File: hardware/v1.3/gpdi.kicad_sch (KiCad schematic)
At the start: 20 parts, among them J2 HDMI_C_1.3, U1 ECP5-CABGA256, U5 PCA9306DC1

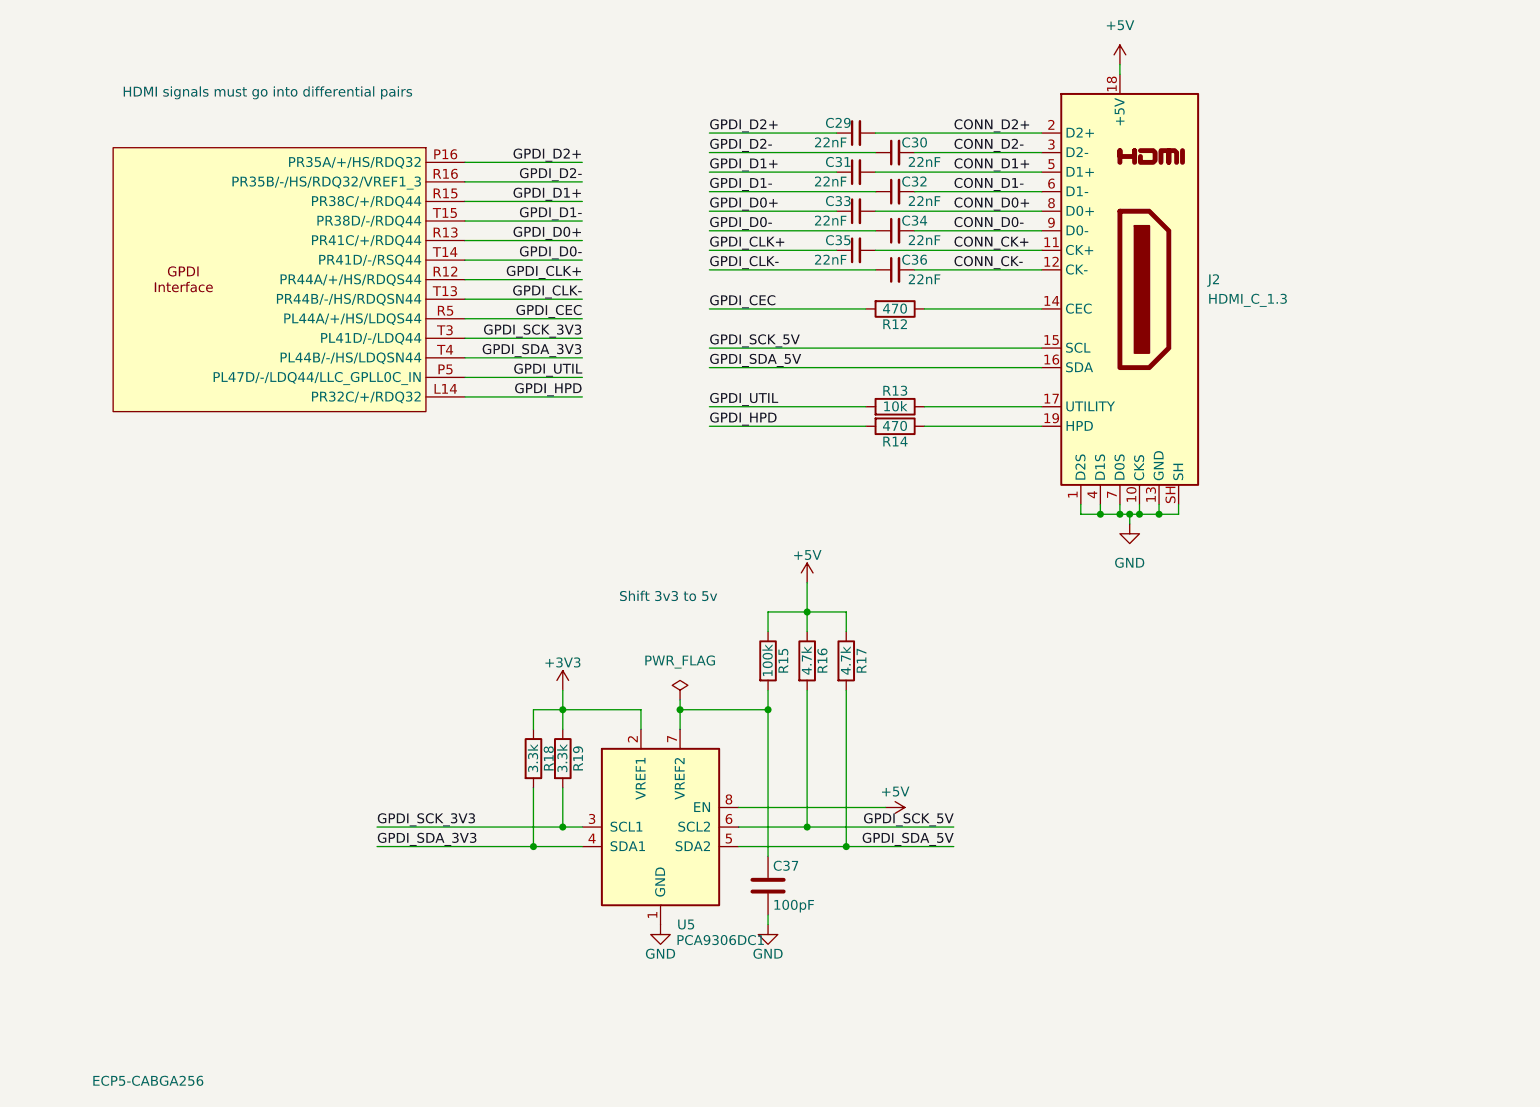
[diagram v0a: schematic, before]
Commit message: Refine README
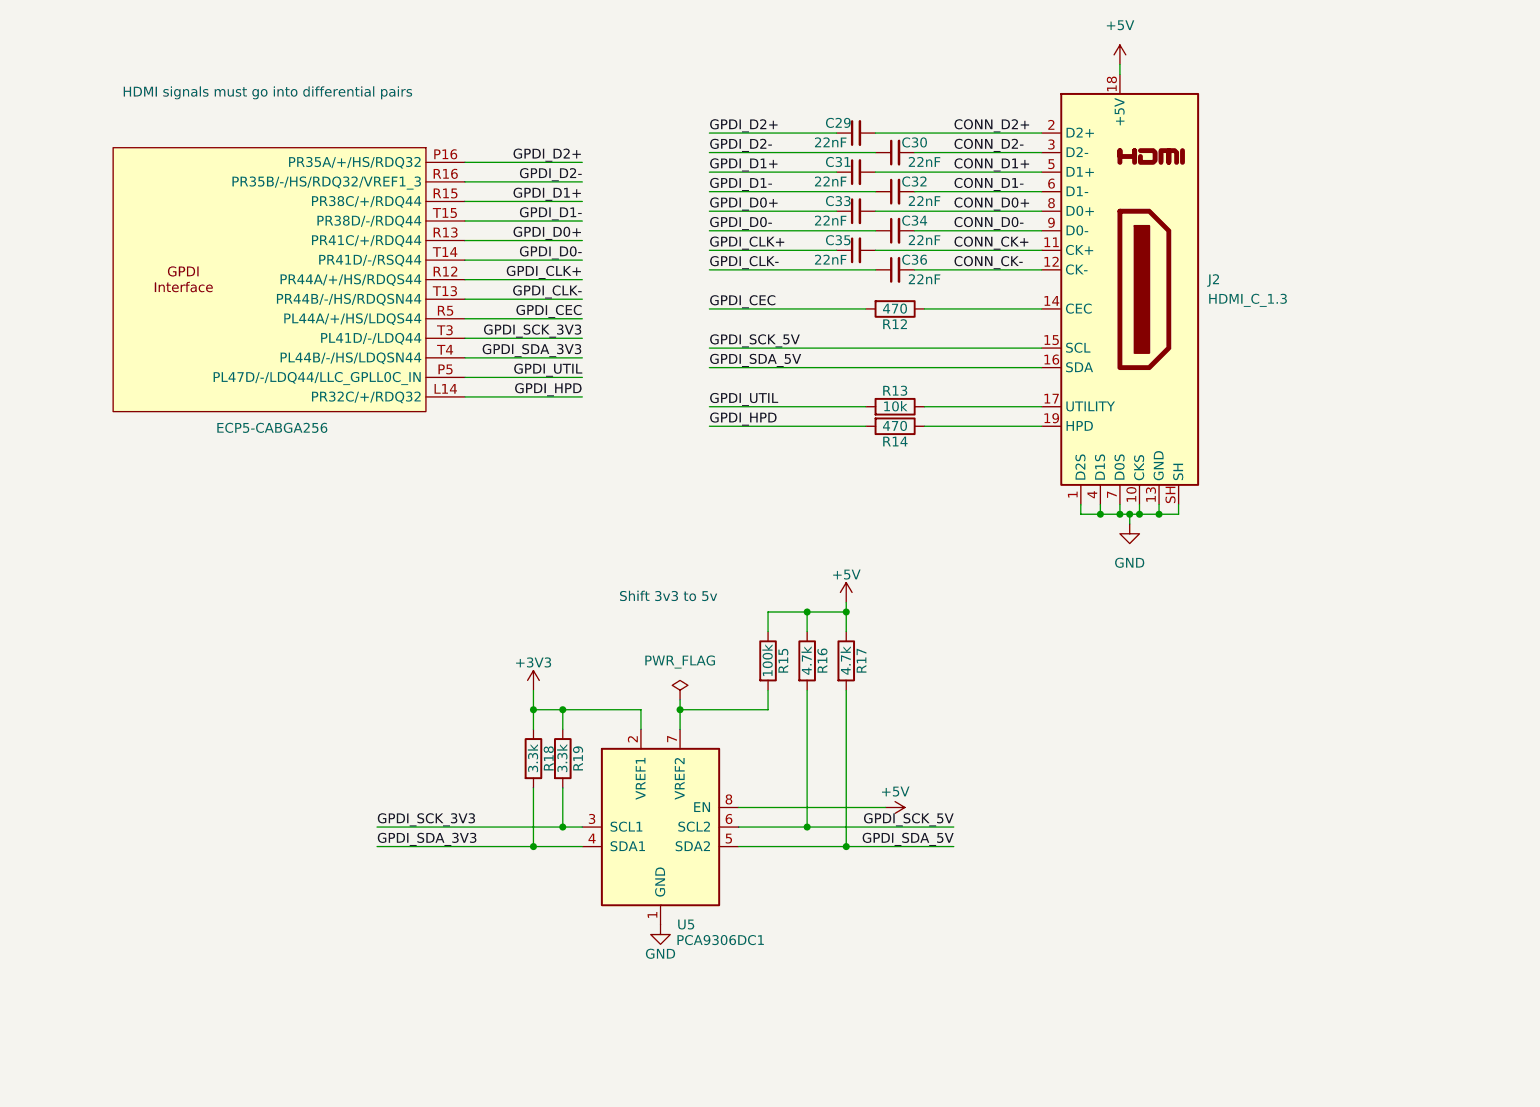
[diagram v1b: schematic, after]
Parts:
- removed C37: 100pF, Capacitor_SMD:C_0402_1005Metric, symbol Device:C
- C29, C30, C31, C32, C33, C34, C35, C36: LCSC Link (none) -> https://lcsc.com/product-detail/Multilayer-Ceramic-Capacito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; Manufactuer Part Number (none) -> 0402B223K500NT
- J2: LCSC Link (none) -> https://lcsc.com/product-detail/HDMI-Connectors_XKB-Connect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; Manufactuer Part Number (none) -> A71-05H4-111N1
- R12, R14: LCSC Link (none) -> https://lcsc.com/product-detail/Chip-Resistor-Surface-Mount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; Manufactuer Part Number (none) -> 0402WGF4700TCE
- R13: LCSC Link (none) -> https://lcsc.com/product-detail/Chip-Resistor-Surface-Mount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; Manufactuer Part Number (none) -> 0402WGF1002TCE
- R15: LCSC Link (none) -> https://lcsc.com/product-detail/Chip-Resistor-Surface-Mount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; Manufactuer Part Number (none) -> 0402WGF1003TCE
- R16, R17: LCSC Link (none) -> https://lcsc.com/product-detail/Chip-Resistor-Surface-Mount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; LCSC Part # C25900 -> C25900; Manufactuer Part Number (none) -> 0402WGF4701TCE
- R18, R19: LCSC Link (none) -> https://lcsc.com/product-detail/Chip-Resistor-Surface-Mount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; LCSC Part # C25890 -> C25890; Manufactuer Part Number (none) -> 0402WGF3301TCE
- U1: LCSC Link (none) -> https://lcsc.com/product-detail/Programmable-Logic-Device-C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; LCSC Part # (none) -> C1521614; Manufactuer Part Number (none) -> LFE5U-25F-6BG256C
- U5: LCSC Link (none) -> https://lcsc.com/product-detail/Translators-Level-Shifters_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; Manufactuer Part Number (none) -> PCA9306DC1

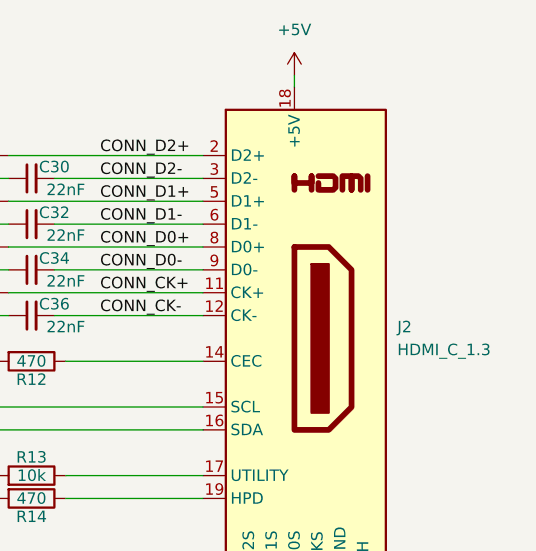
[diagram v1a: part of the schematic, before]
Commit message: Added start of documentation and changed GPDI
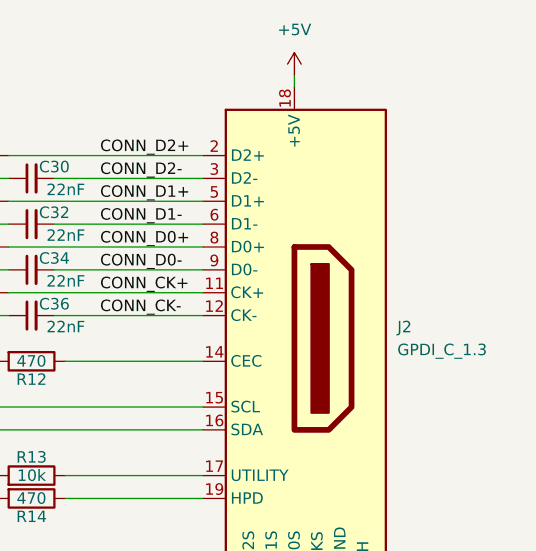
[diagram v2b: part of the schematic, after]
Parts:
- J2: value HDMI_C_1.3 -> GPDI_C_1.3; symbol Connector:HDMI_C_1.3 -> icepi-lib:GPDI_C_1.3
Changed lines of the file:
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@@
 	)
 	(symbol
-		(lib_id "Connector:HDMI_C_1.3")
+		(lib_id "icepi-lib:GPDI_C_1.3")
 		(at 196.85 77.47 0)
 		(unit 1)
@@
 			)
 		)
-		(property "Value" "HDMI_C_1.3"
+		(property "Value" "GPDI_C_1.3"
 			(at 208.28 78.7399 0)
 			(effects
@@
 			)
 		)
-		(property "Datasheet" "http://pinoutguide.com/PortableDevices/mini_hdmi_pinout.shtml"
+		(property "Datasheet" "-"
 			(at 197.485 77.47 0)
 			(effects
@@
 			)
 		)
-		(property "Description" "HDMI 1.3+ type C connector"
+		(property "Description" "GPDI type C connector"
 			(at 196.85 77.47 0)
 			(effects

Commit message: Update files
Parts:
- added U12: TPD2EUSB30A, Package_TO_SOT_SMD:Texas_DRT-3, symbol Power_Protection:TPD2EUSB30A
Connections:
- net GND: now also U12.3 (GND)
- net GPDI_HPD: now also U12.2 (D-)
- net GPDI_UTIL: now also U12.1 (D+)
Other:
- note added: "HDMI signals differential I/O pins"
- note added: "Signal filtering! UwU"
- note added: "Using USB TSV diode to BOM optimize Can be replaced with only one 3.6V zener on HPD line Protect I/O pins from 5V"
- note removed: "HDMI signals must go into differential pairs"
- moved on the sheet: C29, C30, C31, C32, C33, C34, C35, C36, J2, R12, R13, R14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

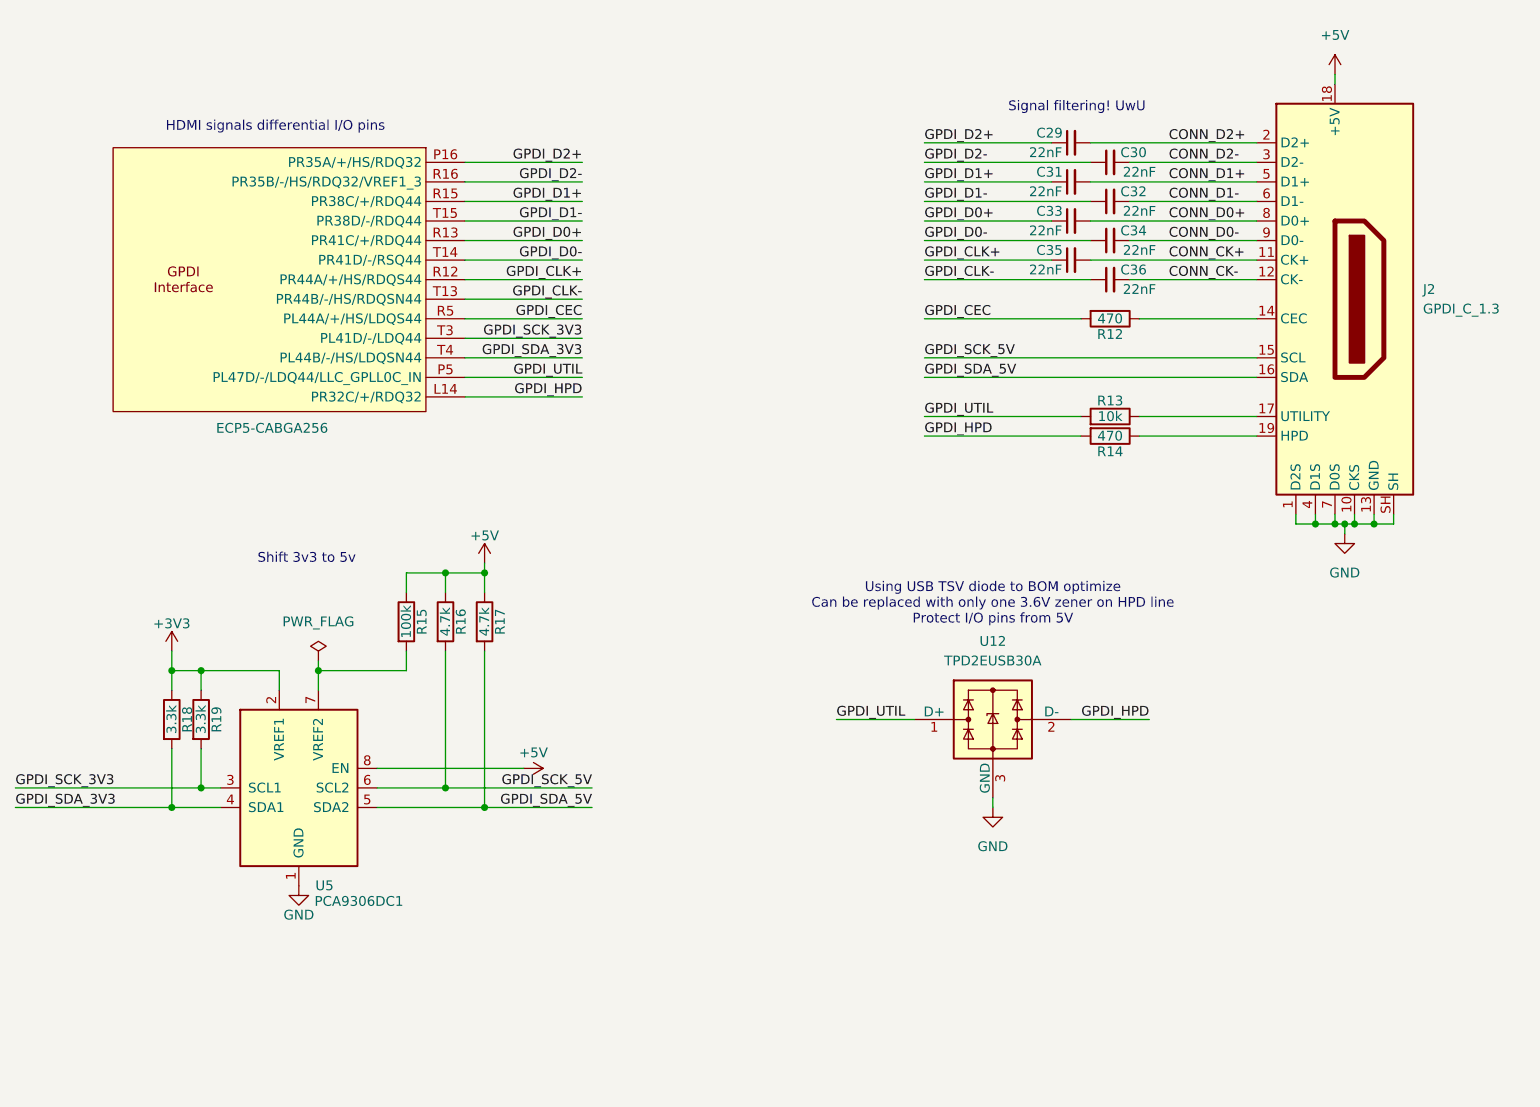
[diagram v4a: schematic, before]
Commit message: Improve makefile and hardware
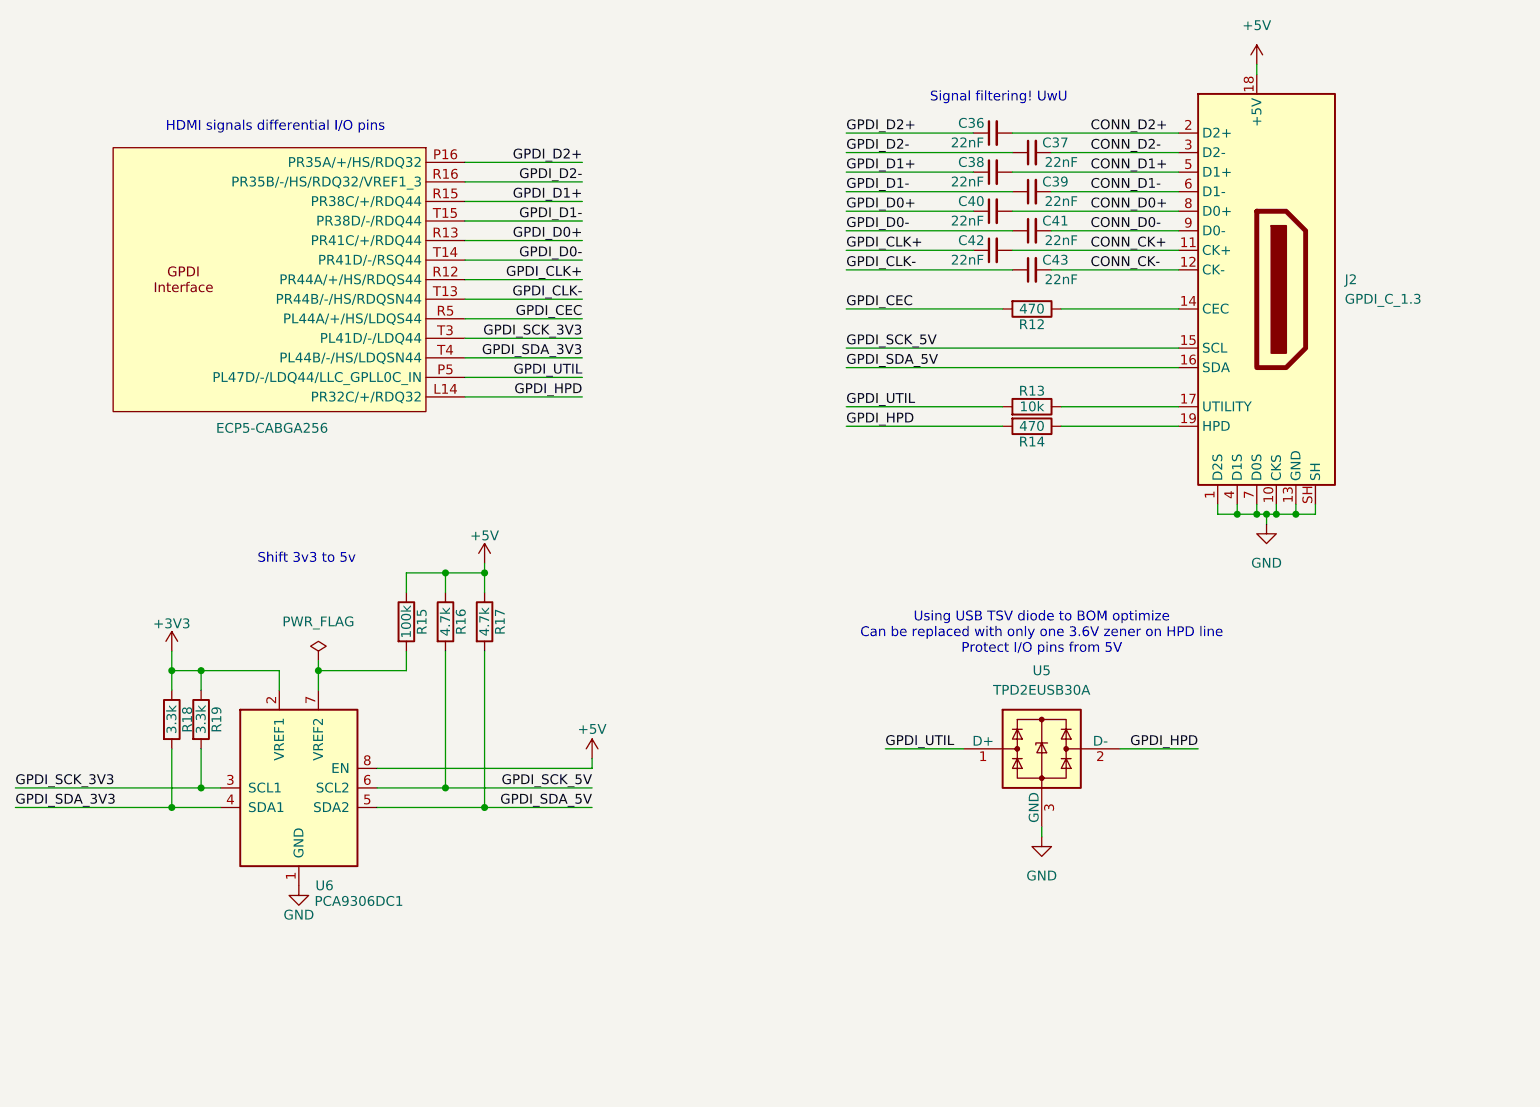
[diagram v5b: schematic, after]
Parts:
- renumbered C29 to C36, C30 to C37, C31 to C38, C32 to C39, C33 to C40, C34 to C41, C35 to C42, C36 to C43, U12 to U5, U5 to U6
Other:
- title: Icepi zero -> Icepi Zero
- moved on the sheet: C36, C37, C38, C39, C40, C41, C42, C43, J2, R12, R13, R14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
